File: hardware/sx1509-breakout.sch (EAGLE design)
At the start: 31 parts, among them U1 SX1509

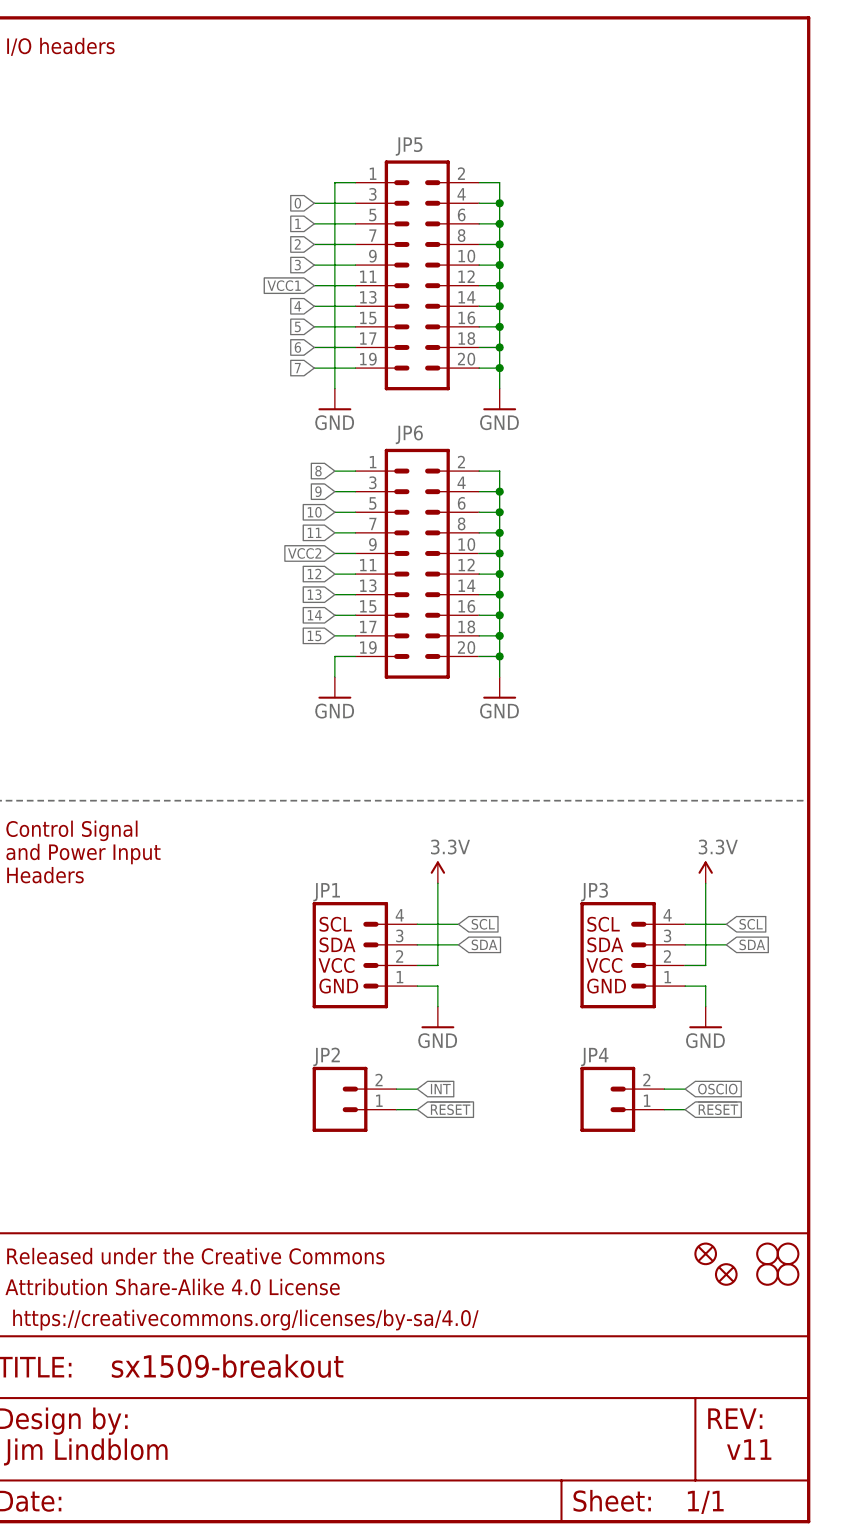
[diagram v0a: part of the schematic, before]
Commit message: Making power busses selectable. Moving silk.
- Not defaulting the two power bus headers to either GND or VCC.
- Adding two jumpers on each header to allow connecting them high or low.
- This will make it easier to set up LEDs as either source or sink.
- It'll also make it easier to short VCC to GND - will require extra
  caution using the jumpers.
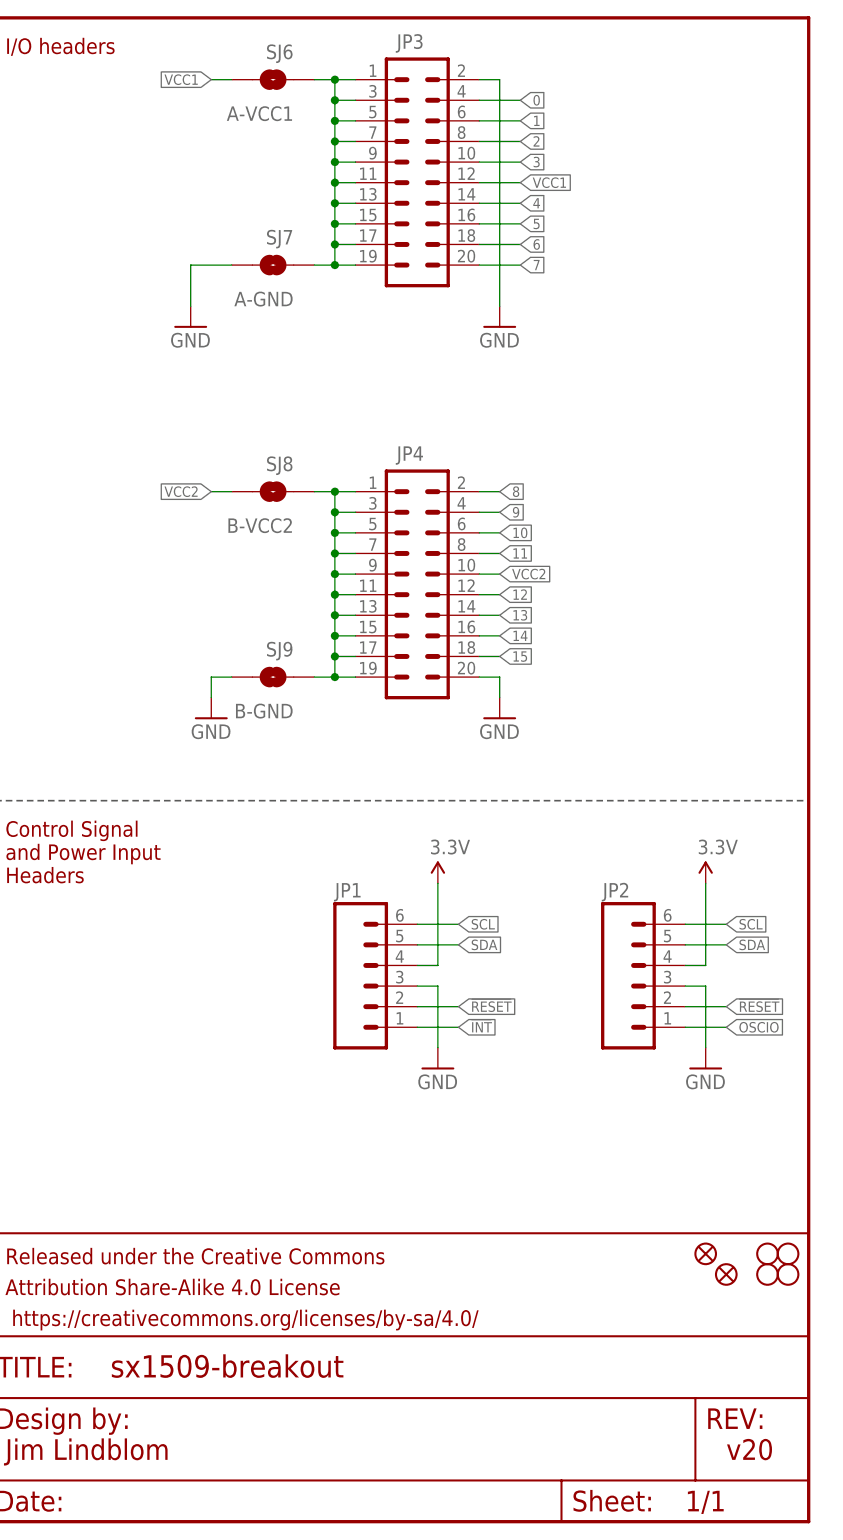
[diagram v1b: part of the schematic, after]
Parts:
- removed JP5, JP6: (no value), SparkFun-Connectors:M10X2NOSILK
- added SJ6: A-VCC1, SparkFun-Passives:JUMPER-PAD-2-NO
- added SJ7: A-GND, SparkFun-Passives:JUMPER-PAD-2-NO
- added SJ8: B-VCC2, SparkFun-Passives:JUMPER-PAD-2-NO
- added SJ9: B-GND, SparkFun-Passives:JUMPER-PAD-2-NO
- JP1: device SparkFun-Connectors:I2C_STANDARD -> SparkFun-Connectors:M06SILK_FEMALE_PTH
- JP2: device SparkFun-Connectors:M02PTH -> SparkFun-Connectors:M06SILK_FEMALE_PTH
- JP3: device SparkFun-Connectors:I2C_STANDARD -> SparkFun-Connectors:M10X2ROUND_NOSILK
- JP4: device SparkFun-Connectors:M02PTH -> SparkFun-Connectors:M10X2ROUND_NOSILK
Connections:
- new net N$3: JP4.1, JP4.11, JP4.13, JP4.15, JP4.17, JP4.19, JP4.3, JP4.5, JP4.7, JP4.9, SJ8.1, SJ9.1
- new net PWRBUSA: JP3.1, JP3.11, JP3.13, JP3.15, JP3.17, JP3.19, JP3.3, JP3.5, JP3.7, JP3.9, SJ6.1, SJ7.1
- net !INT: now also JP1.1; no longer JP2.2
- net !RESET: now also JP1.2, JP2.2; no longer JP2.1, JP4.1
- net 0: now also JP3.4; no longer JP5.3
- net 1: now also JP3.6; no longer JP5.5
- net 10: now also JP4.6; no longer JP6.5
- net 11: now also JP4.8; no longer JP6.7
- net 12: now also JP4.12; no longer JP6.11
- net 13: now also JP4.14; no longer JP6.13
- net 14: now also JP4.16; no longer JP6.15
- net 15: now also JP4.18; no longer JP6.17
- net 2: now also JP3.8; no longer JP5.7
- net 3: now also JP3.10; no longer JP5.9
- net 3.3V: now also JP1.4, JP2.4; no longer JP1.2, JP3.2
- net 4: now also JP3.14; no longer JP5.13
- net 5: now also JP3.16; no longer JP5.15
- net 6: now also JP3.18; no longer JP5.17
- net 7: now also JP3.20; no longer JP5.19
- net 8: now also JP4.2; no longer JP6.1
- net 9: now also JP4.4; no longer JP6.3
- net GND: now also JP1.3, JP2.3, JP3.2, JP4.20, SJ7.2, SJ9.2; no longer JP1.1, JP3.1, JP5.1, JP5.10, JP5.12, JP5.14, JP5.16, JP5.18, JP5.2, JP5.20, JP5.4, JP5.6, JP5.8, JP6.10, JP6.12, JP6.14, JP6.16, JP6.18, JP6.19, JP6.2, JP6.20, JP6.4, JP6.6, JP6.8
- net OSCIO: now also JP2.1; no longer JP4.2
- net SCL: now also JP1.6, JP2.6; no longer JP1.4, JP3.4
- net SDA: now also JP1.5, JP2.5; no longer JP1.3, JP3.3
- net VCC1: now also JP3.12, SJ6.2; no longer JP5.11
- net VCC2: now also JP4.10, SJ8.2; no longer JP6.9
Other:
- note added: "v20"
- note removed: "v11"

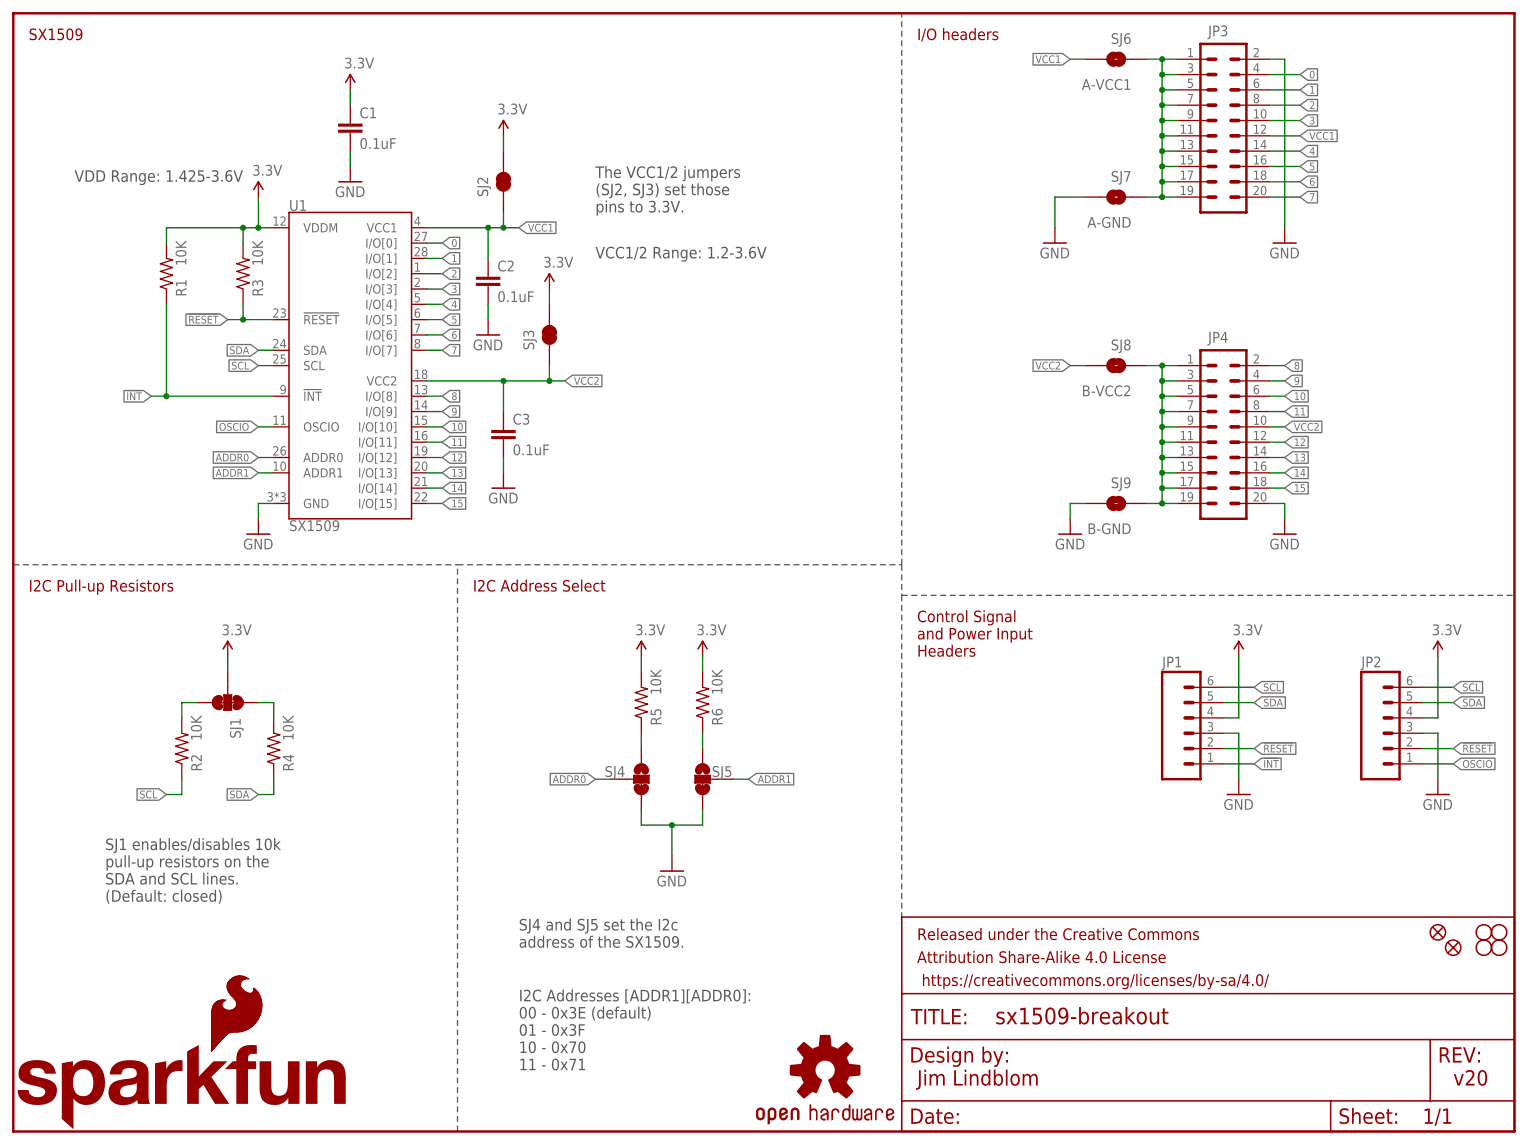
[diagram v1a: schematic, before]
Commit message: Defaulting power busses to GND. Moving SJ2&3.
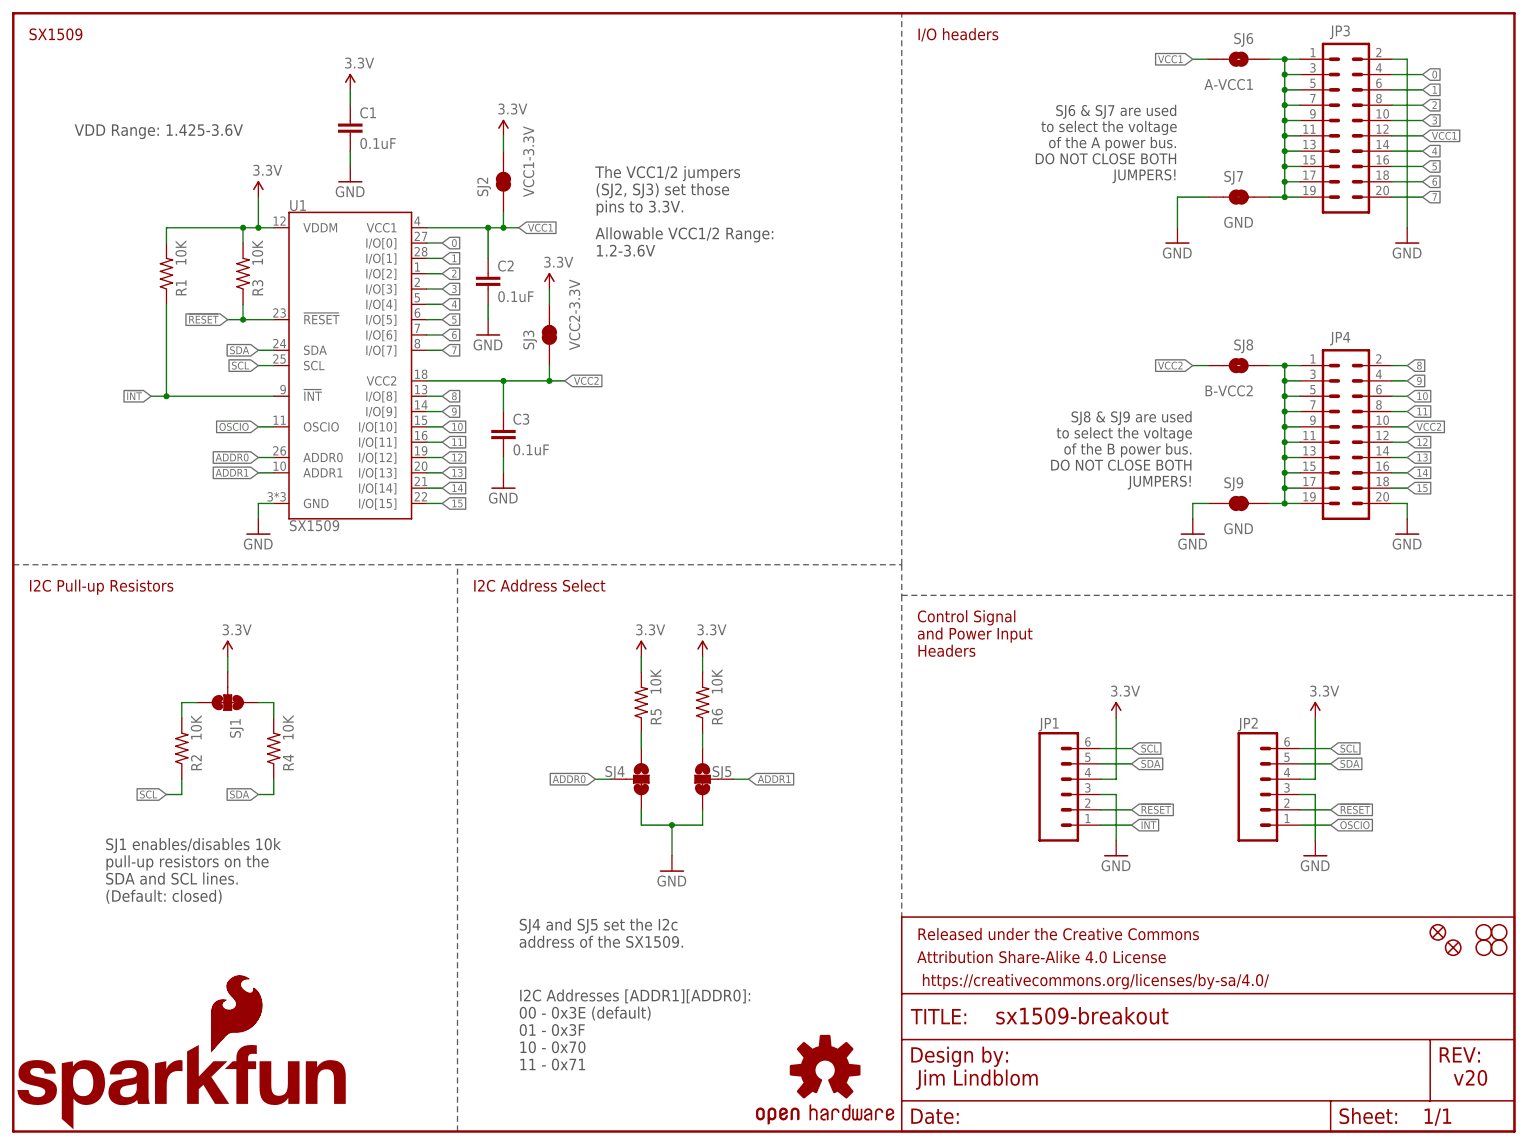
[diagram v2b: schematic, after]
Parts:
- SJ2: value JUMPER-PAD-2-NC_BY_TRACE -> VCC1-3.3V
- SJ3: value JUMPER-PAD-2-NC_BY_TRACE -> VCC2-3.3V
- SJ7: value A-GND -> GND; device SparkFun-Passives:JUMPER-PAD-2-NO -> SparkFun-Passives:JUMPER-PAD-2-NC_BY_TRACENO_SILK
- SJ9: value B-GND -> GND; device SparkFun-Passives:JUMPER-PAD-2-NO -> SparkFun-Passives:JUMPER-PAD-2-NC_BY_TRACENO_SILK
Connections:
- net GND: now also SJ7.1, SJ9.1; no longer SJ7.2, SJ9.2
- net N$3: now also SJ9.2; no longer SJ9.1
- net PWRBUSA: now also SJ7.2; no longer SJ7.1
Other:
- note added: "Allowable VCC1/2 Range: 1.2-3.6V"
- note added: "SJ6 & SJ7 are used to select the voltage of the A power bus. DO NOT CLOSE BOTH JUMPERS!"
- note added: "SJ8 & SJ9 are used to select the voltage of the B power bus. DO NOT CLOSE BOTH JUMPERS!"
- note removed: "VCC1/2 Range: 1.2-3.6V"
- moved on the sheet: JP1, JP2, JP3, JP4, SJ6, SJ8
